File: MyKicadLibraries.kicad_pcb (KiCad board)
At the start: 2 copper layers, 184.4 x 134.7 mm, 43 parts, among them J1 Conn_01x08, J10 RCJ-22, J11 DIN-5, J12 Mini-DIN-6, J13 USB_A, J14 Conn_01x02, J15 Conn_01x02, J2 Conn_01x08, J3 POGO Pins, J4 c8-inlet, J5 FTDI, J6 Micro_SD_Card, J7 Conn_01x04, J8 Conn_02x04_Counter_Clockwise, J9 Conn_01x04, SW1 Schurter Switch, SW2 POWER, U1 radio-receiver, U10 rdm-6300, U11 magnetic-charger, U12 adafruit-MAX98357, U13 TTL, U14 lxb18, U15 esp32-wemos-d1-mini, U16 TCRT5000, U17 opb607a, U18 max98367, U19 esp-01f, U2 tp4056, U20 m18, U21 bme280, U23 mems-mic, U3 LilygoSIMT7000G, U4 esp-01m, U5 relais_module, U6 ESP-01, U7 dcdc, U8 mems-mic, U9 ESP-12E

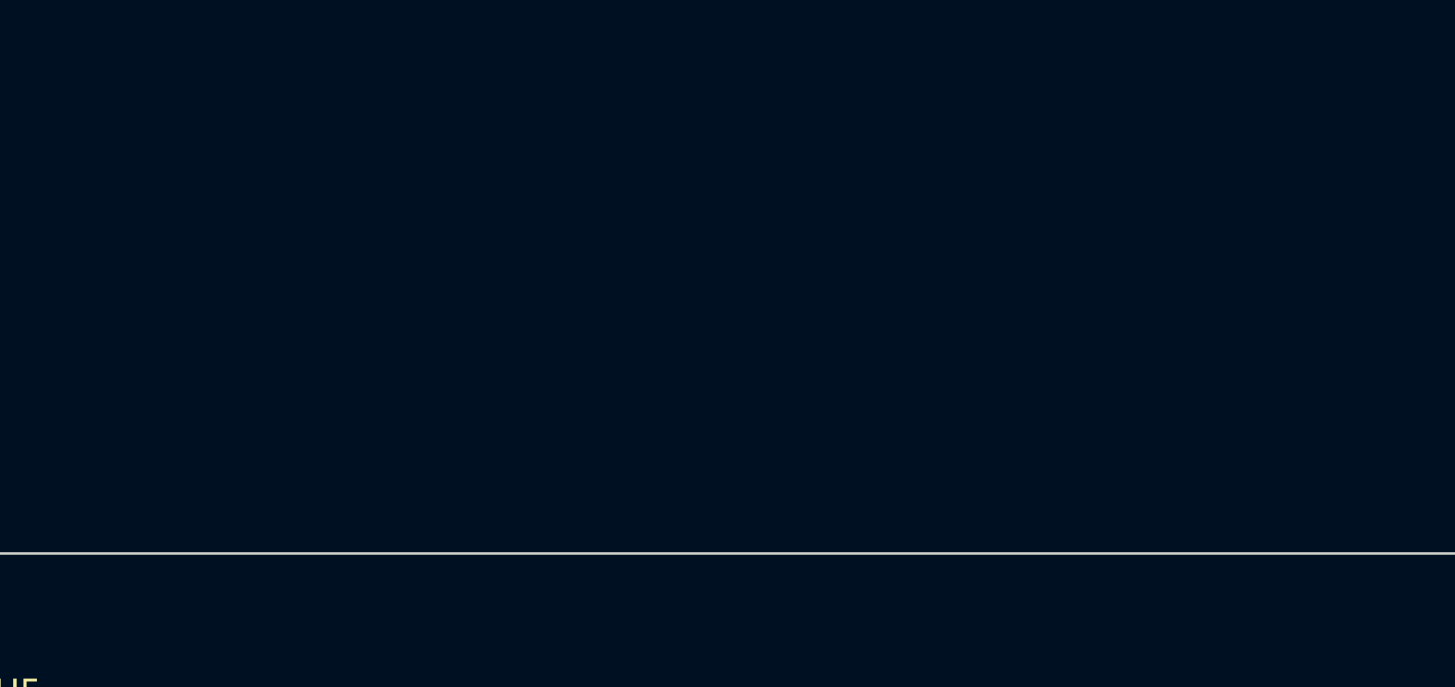
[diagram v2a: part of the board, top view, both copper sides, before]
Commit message: Add ld2450
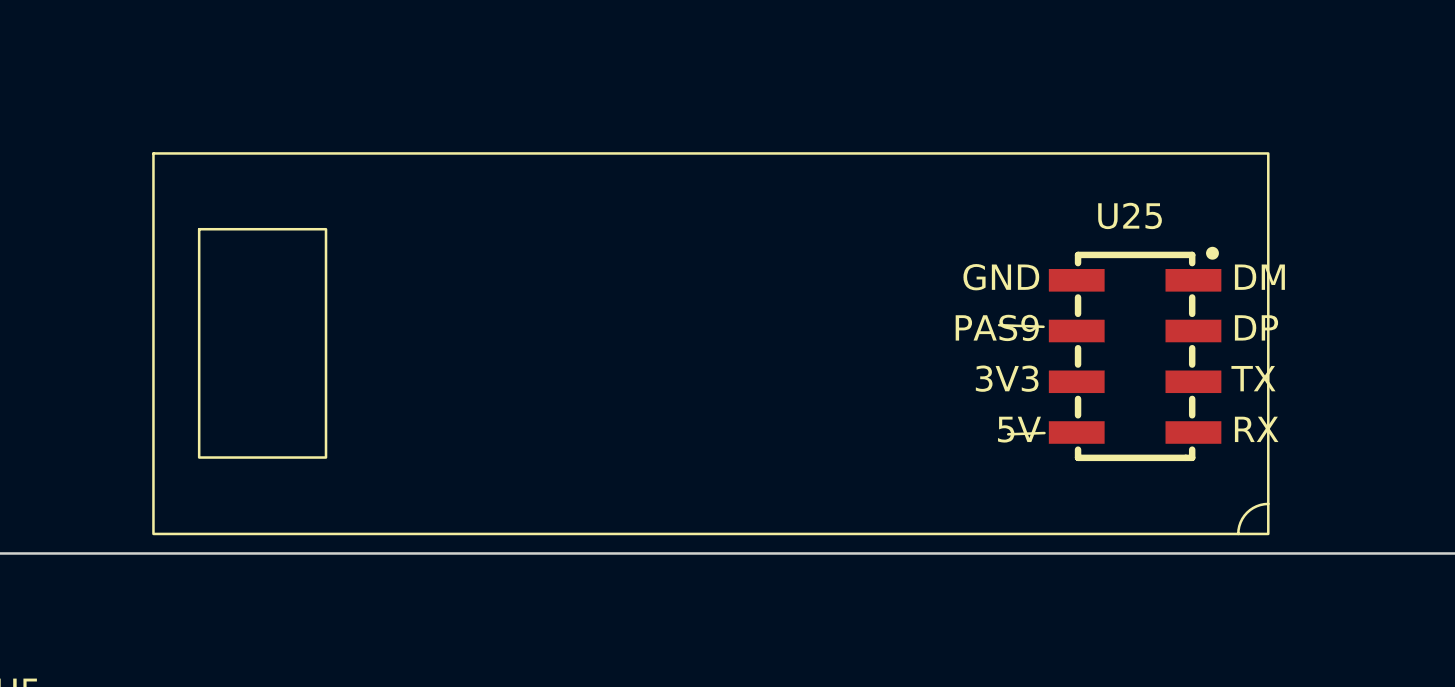
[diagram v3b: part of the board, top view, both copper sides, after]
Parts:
- added U25: ~, ld2450:ld2450, F.Cu at (165.8, 25.0)
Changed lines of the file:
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@@
   (net 305 "unconnected-(U24-GND-Pad5)")
   (net 306 "unconnected-(U24-VOUT-Pad6)")
+  (net 307 "unconnected-(U25-DM-Pad1)")
+  (net 308 "unconnected-(U25-DP-Pad2)")
+  (net 309 "unconnected-(U25-TX-Pad3)")
+  (net 310 "unconnected-(U25-RX-Pad4)")
+  (net 311 "unconnected-(U25-5V-Pad5)")
+  (net 312 "unconnected-(U25-3V3-Pad6)")
+  (net 313 "unconnected-(U25-PA9-Pad7)")
+  (net 314 "unconnected-(U25-GND-Pad8)")
   (footprint "esp-01f:esp-01f" (layer "F.Cu")
     (at 114.405 137.985)
@@
     )
   )
+  (footprint "ld2450:ld2450" (layer "F.Cu")
+    (at 165.75 25)
+    (property "Sheetfile" "MyKicadLibraries.kicad_sch")
+    (property "Sheetname" "")
+    (attr through_hole)
+    (fp_text reference "U25" (at -0.25 -5.5 unlocked) (layer "F.SilkS")
+        (effects (font (size 1 1) (thickness 0.1)))
+    )
+    (fp_text value "~" (at 0 7 unlocked) (layer "F.Fab")
+        (effects (font (size 1 1) (thickness 0.15)))
+    )
+    (fp_text user "5V" (at -3.75 3.5 unlocked) (layer "F.SilkS")
+        (effects (font (size 1 1) (thickness 0.1)) (justify right bottom))
+    )
+    (fp_text user "RX" (at 3.75 3.5 unlocked) (layer "F.SilkS")
+        (effects (font (size 1 1) (thickness 0.1)) (justify left bottom))
+    )
+    (fp_text user "DM" (at 3.75 -2.5 unlocked) (layer "F.SilkS")
+        (effects (font (size 1 1) (thickness 0.1)) (justify left bottom))
+    )
+    (fp_text user "DP" (at 3.75 -0.5 unlocked) (layer "F.SilkS")
+        (effects (font (size 1 1) (thickness 0.1)) (justify left bottom))
+    )
+    (fp_text user "3V3" (at -3.75 1.5 unlocked) (layer "F.SilkS")
+        (effects (font (size 1 1) (thickness 0.1)) (justify right bottom))
+    )
+    (fp_text user "TX" (at 3.75 1.5 unlocked) (layer "F.SilkS")
+        (effects (font (size 1 1) (thickness 0.1)) (justify left bottom))
+    )
+    (fp_text user "GND" (at -3.75 -2.5 unlocked) (layer "F.SilkS")
+        (effects (font (size 1 1) (thickness 0.1)) (justify right bottom))
+    )
+    (fp_text user "PAS9" (at -3.75 -0.5 unlocked) (layer "F.SilkS")
+        (effects (font (size 1 1) (thickness 0.1)) (justify right bottom))
+    )
+    (fp_text user "REF**" (at -0.25 -5.5) (layer "F.Fab")
+        (effects (font (size 1 1) (thickness 0.15)))
+    )
+    (fp_text user "${REFERENCE}" (at 0 5.5 unlocked) (layer "F.Fab")
+        (effects (font (size 1 1) (thickness 0.15)))
+    )
+    (fp_line (start -5.410206 -1.230475) (end -3.66082 -1.166628)
+      (stroke (width 0.1) (type default)) (layer "F.SilkS"))
+    (fp_line (start -5.052668 3.07276) (end -3.623942 3.022226)
+      (stroke (width 0.1) (type default)) (layer "F.SilkS"))
+    (fp_line (start -2.299962 -4) (end -2.299962 -3.676124)
+      (stroke (width 0.254) (type solid)) (layer "F.SilkS"))
+    (fp_line (start -2.299962 -2.323851) (end -2.299962 -1.676124)
+      (stroke (width 0.254) (type solid)) (layer "F.SilkS"))
+    (fp_line (start -2.299962 -0.323851) (end -2.299962 0.323876)
+      (stroke (width 0.254) (type solid)) (layer "F.SilkS"))
+    (fp_line (start -2.299962 1.676149) (end -2.299962 2.323876)
+      (stroke (width 0.254) (type solid)) (layer "F.SilkS"))
+    (fp_line (start -2.299962 3.676149) (end -2.299962 4)
+      (stroke (width 0.254) (type solid)) (layer "F.SilkS"))
+    (fp_line (start -2.299962 4) (end 1.950025 4)
+      (stroke (width 0.254) (type solid)) (layer "F.SilkS"))
+    (fp_line (start 1.950025 4) (end 2.200038 4)
+      (stroke (width 0.254) (type solid)) (layer "F.SilkS"))
+    (fp_line (start 2.200038 -4) (end -2.299962 -4)
+      (stroke (width 0.254) (type solid)) (layer "F.SilkS"))
+    (fp_line (start 2.200038 -3.676124) (end 2.200038 -4)
+      (stroke (width 0.254) (type solid)) (layer "F.SilkS"))
+    (fp_line (start 2.200038 -2.323851) (end 2.200038 -1.676124)
+      (stroke (width 0.254) (type solid)) (layer "F.SilkS"))
+    (fp_line (start 2.200038 -0.323851) (end 2.200038 0.323876)
+      (stroke (width 0.254) (type solid)) (layer "F.SilkS"))
+    (fp_line (start 2.200038 1.676149) (end 2.200038 2.323876)
+      (stroke (width 0.254) (type solid)) (layer "F.SilkS"))
+    (fp_line (start 2.200038 4) (end 2.200038 3.676149)
+      (stroke (width 0.254) (type solid)) (layer "F.SilkS"))
+    (fp_rect (start -38.75 -8) (end 5.2 7)
+      (stroke (width 0.1) (type default)) (fill none) (layer "F.SilkS"))
+    (fp_rect (start -36.947654 -5.012823) (end -31.947654 3.987177)
+      (stroke (width 0.1) (type default)) (fill none) (layer "F.SilkS"))
+    (fp_arc (start 4.016912 7) (mid 4.362027 6.164836) (end 5.196027 5.816919)
+      (stroke (width 0.1) (type default)) (layer "F.SilkS"))
+    (fp_circle (center 3 -4.06604) (end 3 -4.036068)
+      (stroke (width 0.059995) (type solid)) (fill none) (layer "F.SilkS"))
+    (fp_circle (center 3 -4.06604) (end 3 -3.93904)
+      (stroke (width 0.254) (type solid)) (fill none) (layer "F.SilkS"))
+    (pad "1" smd rect (at 2.25 -3 270) (size 0.889992 2.2) (layers "F.Cu" "F.Paste" "F.Mask")
+      (net 307 "unconnected-(U25-DM-Pad1)") (pinfunction "DM") (pintype "bidirectional"))
+    (pad "2" smd rect (at 2.25 -1 270) (size 0.889992 2.2) (layers "F.Cu" "F.Paste" "F.Mask")
+      (net 308 "unconnected-(U25-DP-Pad2)") (pinfunction "DP") (pintype "bidirectional"))
+    (pad "3" smd rect (at 2.25 1 270) (size 0.889992 2.2) (layers "F.Cu" "F.Paste" "F.Mask")
+      (net 309 "unconnected-(U25-TX-Pad3)") (pinfunction "TX") (pintype "output"))
+    (pad "4" smd rect (at 2.25 3 270) (size 0.889992 2.2) (layers "F.Cu" "F.Paste" "F.Mask")
+      (net 310 "unconnected-(U25-RX-Pad4)") (pinfunction "RX") (pintype "input"))
+    (pad "5" smd rect (at -2.34995 3 270) (size 0.889992 2.2) (layers "F.Cu" "F.Paste" "F.Mask")
+      (net 311 "unconnected-(U25-5V-Pad5)") (pinfunction "5V") (pintype "power_in"))
+    (pad "6" smd rect (at -2.34995 1 270) (size 0.889992 2.2) (layers "F.Cu" "F.Paste" "F.Mask")
+      (net 312 "unconnected-(U25-3V3-Pad6)") (pinfunction "3V3") (pintype "power_out"))
+    (pad "7" smd rect (at -2.34995 -1 270) (size 0.889992 2.2) (layers "F.Cu" "F.Paste" "F.Mask")
+      (net 313 "unconnected-(U25-PA9-Pad7)") (pinfunction "PA9") (pintype "bidirectional"))
+    (pad "8" smd rect (at -2.34995 -3 270) (size 0.889992 2.2) (layers "F.Cu" "F.Paste" "F.Mask")
+      (net 314 "unconnected-(U25-GND-Pad8)") (pinfunction "GND") (pintype "power_in"))
+    (model "${KIPRJMOD}/lib/ld2450/HLK-LD2450.step"
+      (offset (xyz -17 0.5 7.1))
+      (scale (xyz 1 1 1))
+      (rotate (xyz 90 180 180))
+    )
+    (model "${KIPRJMOD}/lib/ld2450/SMD_8P-P2.00.step"
+      (offset (xyz 0 0 0.25))
+      (scale (xyz 1 1 1))
+      (rotate (xyz 0 0 90))
+    )
+  )

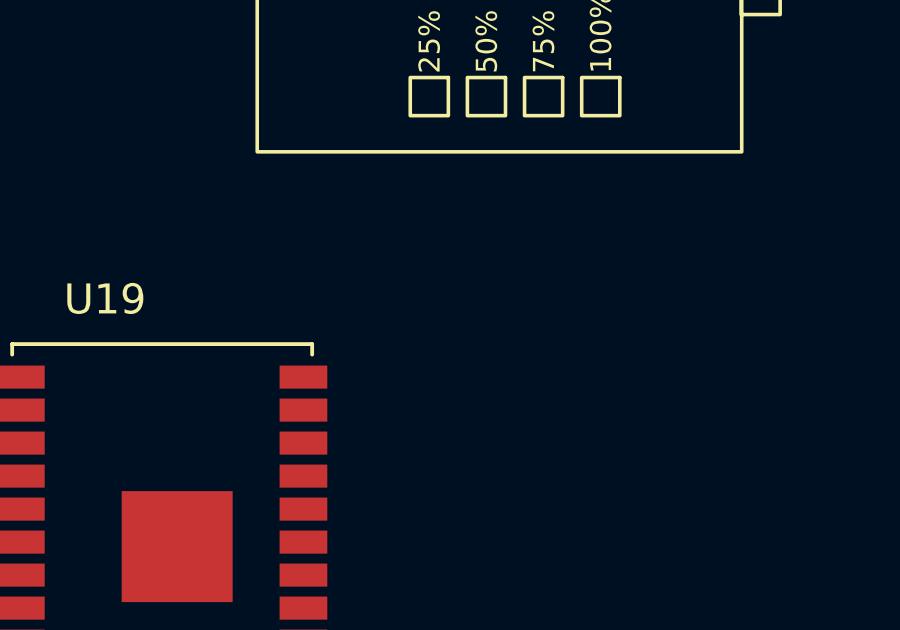
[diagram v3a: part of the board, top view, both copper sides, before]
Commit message: Add Lolin C3 Footprint
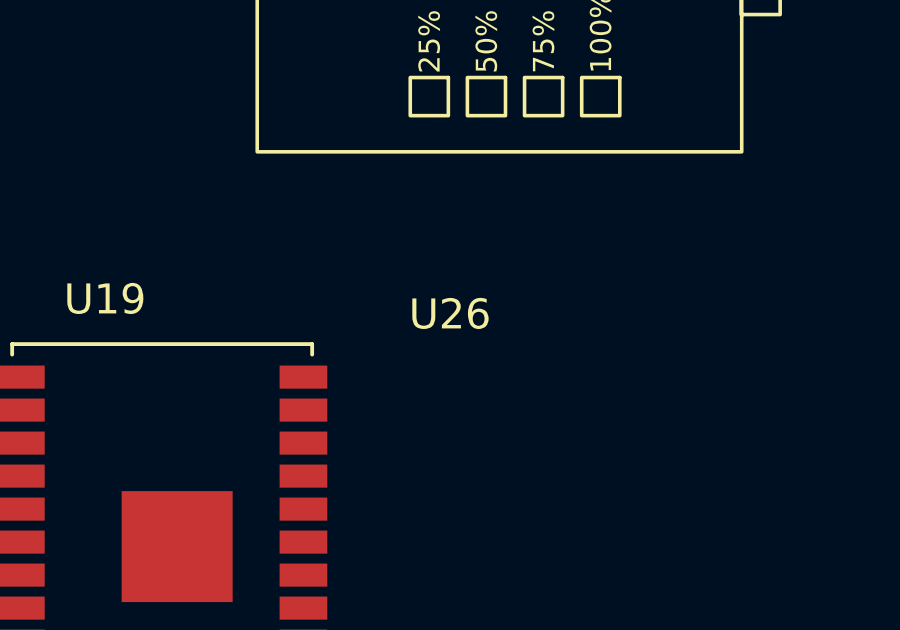
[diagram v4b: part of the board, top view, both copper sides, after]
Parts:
- added U26: ~, c3-pico:c3-pico, F.Cu at (124.0, 132.0)
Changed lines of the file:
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@@
   (net 313 "unconnected-(U25-PA9-Pad7)")
   (net 314 "unconnected-(U25-GND-Pad8)")
+  (footprint "c3-pico:c3-pico" (layer "F.Cu")
+    (at 124 132)
+    (property "Sheetfile" "MyKicadLibraries.kicad_sch")
+    (property "Sheetname" "")
+    (attr through_hole)
+    (fp_text reference "U26" (at 0 -0.5 unlocked) (layer "F.SilkS")
+        (effects (font (size 1 1) (thickness 0.1)))
+    )
+    (fp_text value "~" (at 0 1 unlocked) (layer "F.Fab")
+        (effects (font (size 1 1) (thickness 0.15)))
+    )
+    (fp_text user "${REFERENCE}" (at 0 2.5 unlocked) (layer "F.Fab")
+        (effects (font (size 1 1) (thickness 0.15)))
+    )
+  )
   (footprint "esp-01f:esp-01f" (layer "F.Cu")
     (at 114.405 137.985)

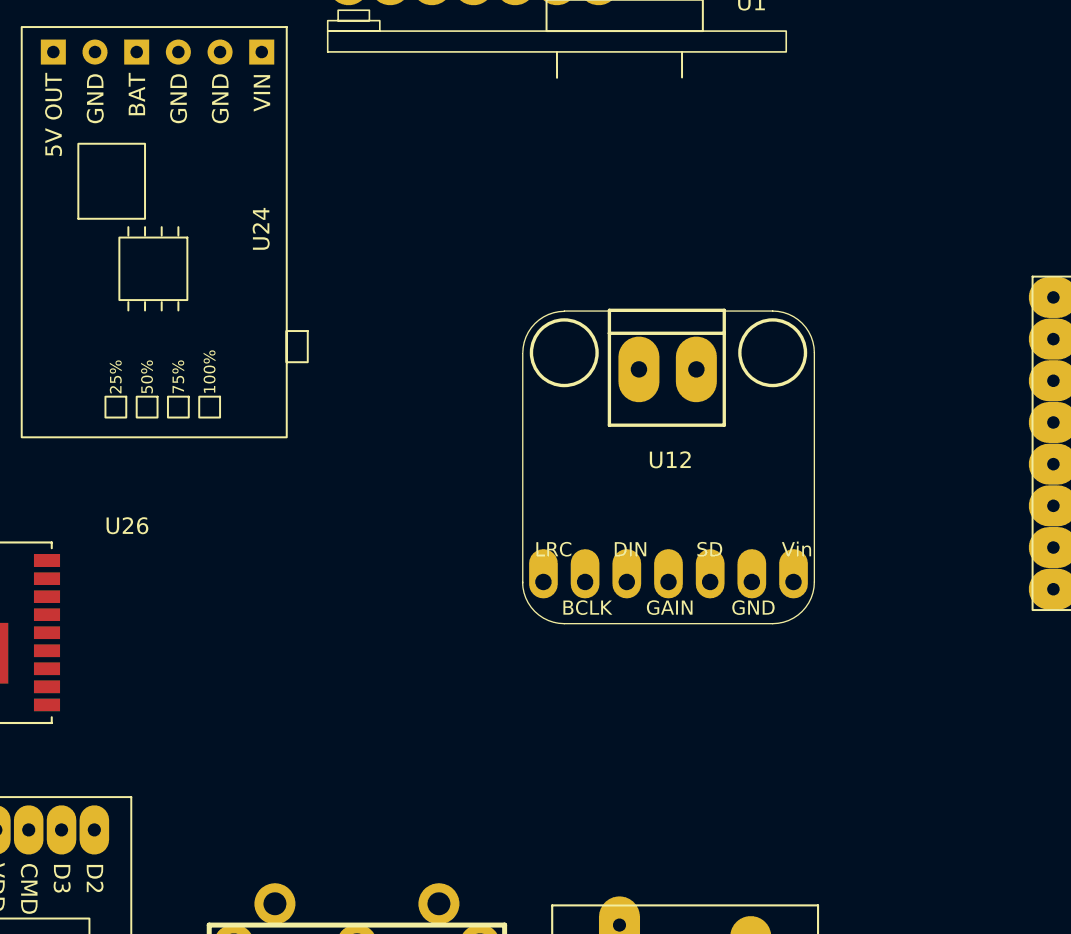
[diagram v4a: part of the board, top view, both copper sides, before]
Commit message: Update Lolin c3 pico component
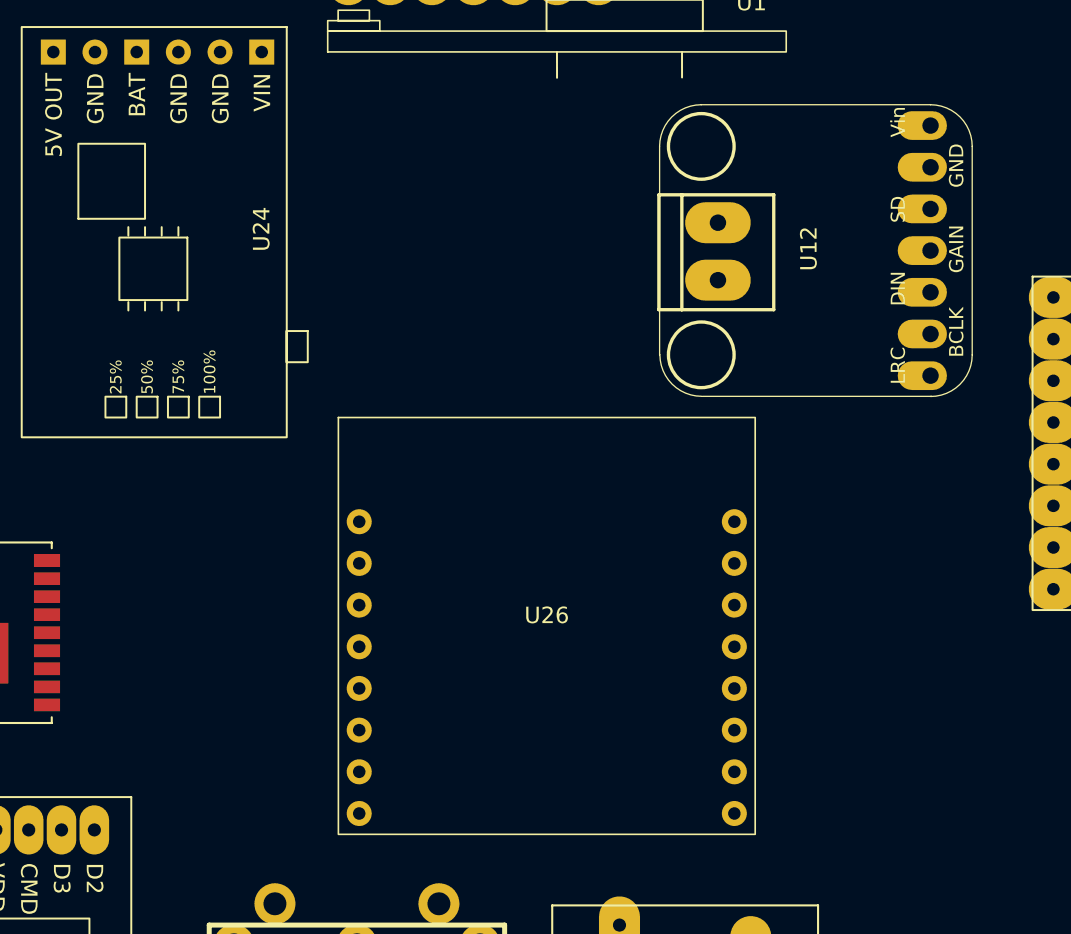
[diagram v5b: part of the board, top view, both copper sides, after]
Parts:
- U26: value ~ -> C3 Pico
- moved U26 26.2 mm to (149.6, 137.6)
- moved U12 16.1 mm to (166.0, 114.6), turned to 90 degrees
